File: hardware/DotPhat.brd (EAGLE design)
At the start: 30 x 65 mm, 17 parts, among them J2 RASPBERRYPI-40-PIN-GPIO_PTH, U1 ATMEGA328P-MU-QFN32

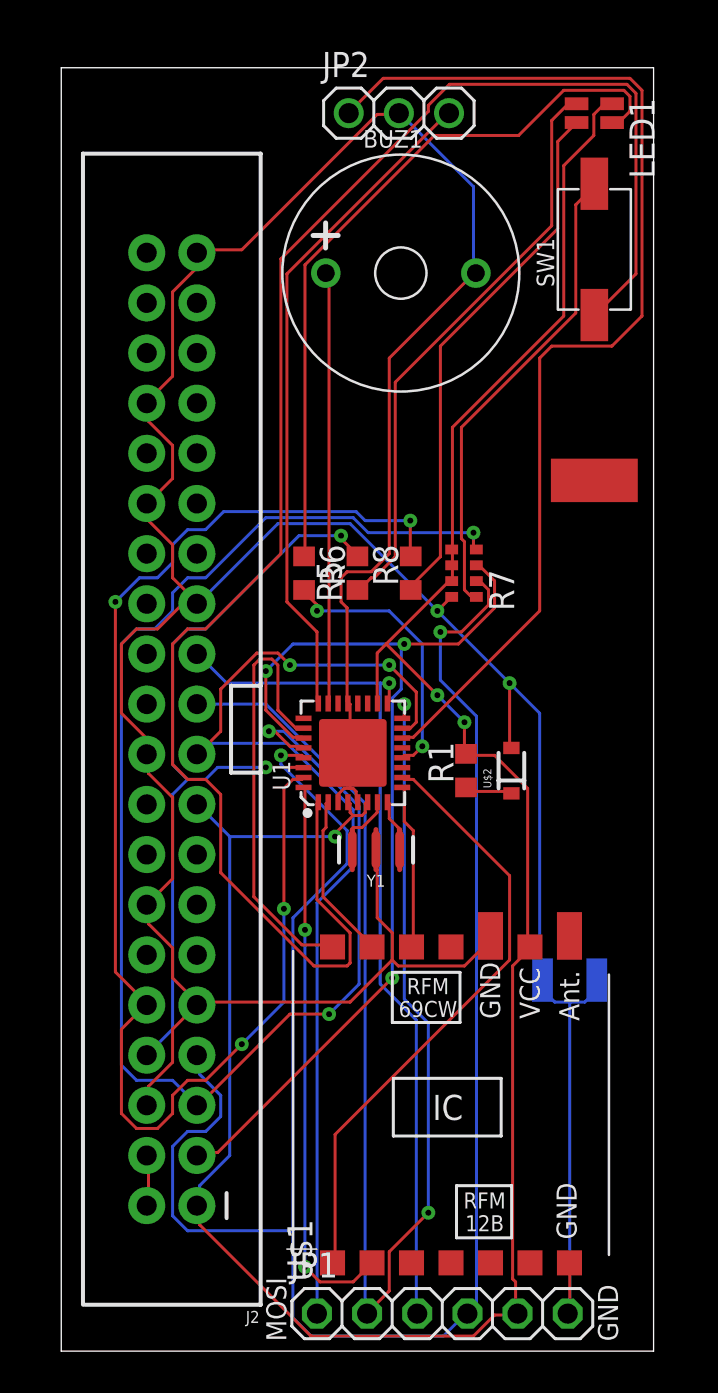
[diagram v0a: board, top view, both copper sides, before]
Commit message: Add 2 out JST connectors, solid GND vias
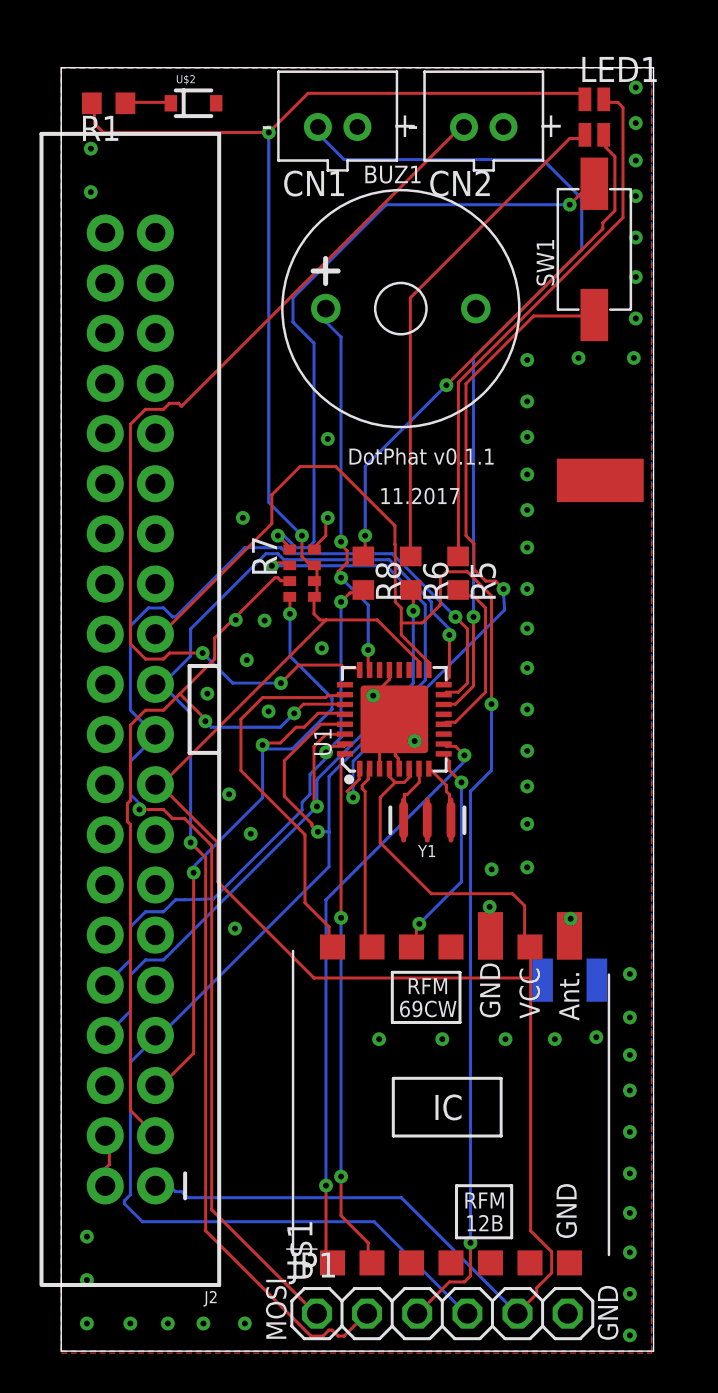
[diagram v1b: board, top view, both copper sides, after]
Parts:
- removed JP2: (no value), adafruit:1X03
- added CN1, CN2: (no value), adafruit:JST-PH-2-THM
- moved R1 38.3 mm to (2.40, 63.2), turned to 180 degrees
- moved U$2 37.4 mm to (6.70, 63.2), turned to 0 degrees
- moved R7 8.20 mm to (12.2, 39.4), turned to 270 degrees
- moved R5 7.80 mm to (20.1, 39.4)
- moved Y1 3.00 mm to (18.5, 26.9)
- moved U1 2.70 mm to (16.9, 32.0)
- moved R6 2.70 mm to (17.7, 39.4), turned to 270 degrees
- moved LOGO1 2.52 mm to (12.2, 44.1), turned to 0 degrees
- moved R8 2.40 mm to (15.3, 39.4), turned to 270 degrees
- moved J2 2.33 mm to (3.50, 32.5)
- moved BUZ1 1.80 mm to (17.2, 52.8)
- moved LED1 0.20 mm to (27.0, 62.5), turned to 0 degrees
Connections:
- net GND: now also CN1.1, CN2.1; no longer JP2.2
- net OUTA: now also CN1.2; no longer JP2.1
- net OUTB: now also CN2.2; no longer JP2.3
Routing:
- net GND: track 193.6 -> 11.0 mm, vias 2 -> 58
- net PUSH: track 87.0 -> 35.0 mm, vias 0 -> 2
- net TXD: track 70.3 -> 28.6 mm, vias 4 -> 2
- net SCL: track 76.3 -> 35.5 mm
- net +3V3: track 124.5 -> 153.1 mm, vias 3 -> 2
- net SCK: track 44.1 -> 71.1 mm, vias 1 -> 2
- net RST: track 98.7 -> 74.9 mm
- net OUTB: track 34.0 -> 47.6 mm, vias 0 -> 2
- net MOSI: track 53.5 -> 65.9 mm
- net OUTA: track 55.8 -> 43.9 mm, vias 0 -> 1
- net N$5: track 24.1 -> 33.7 mm, vias 0 -> 2
- net N$15: track 36.9 -> 27.4 mm
- net SDA: track 50.7 -> 43.0 mm
- net MISO: track 69.9 -> 63.3 mm
- net RXD: track 40.3 -> 34.6 mm
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- added copper zone on layer 1, net GND
- added copper zone on layer 16, net GND
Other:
- board text added: "11.2017"
- board text added: "DotPhat v0.1.1"

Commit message: Replace JST2 with JST4, add leds for channels
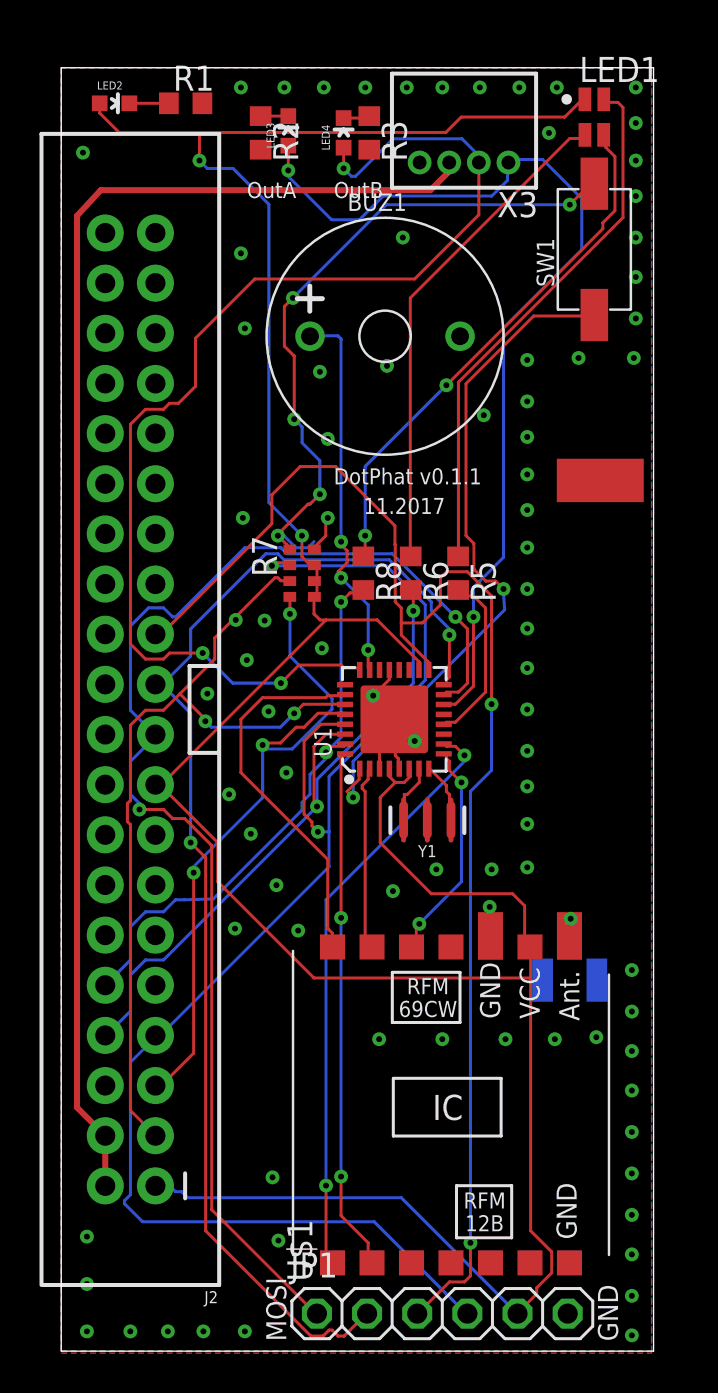
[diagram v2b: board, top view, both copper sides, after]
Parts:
- removed CN1, CN2: (no value), adafruit:JST-PH-2-THM
- removed U$2: DIODE-ZENER-BZT52, SparkFun:SOD-323
- added LED2, LED3, LED4: (no value), SparkFun:LED-0603
- added R2, R3: 250Ω, resistor:R0603
- added X3: S4B-ZR, con-jst:S4B-ZR
- R1: value (none) -> 250Ω
- moved R1 3.90 mm to (6.30, 63.2), turned to 0 degrees
- moved BUZ1 1.61 mm to (16.4, 51.4)
- moved LOGO1 1.39 mm to (10.9, 43.6)
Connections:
- removed net 5V: J2.2, J2.4
- new net +5V: J2.2, J2.4, X3.3
- new net N$7: LED3.C, R2.1
- new net N$9: LED4.C, R3.1
- net +3V3: now also LED2.A; no longer R1.2
- net GND: now also R1.2, R2.2, R3.2, X3.4; no longer CN1.1, CN2.1, U$2.2
- net N$2: now also LED2.C; no longer U$2.1
- net OUTA: now also LED3.A, X3.1; no longer CN1.2
- net OUTB: now also LED4.A, X3.2; no longer CN2.2
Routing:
- net +5V: track 0.00 -> 70.0 mm
- net OUTB: track 47.6 -> 60.0 mm, vias 2 -> 3
- net OUTA: track 43.9 -> 48.8 mm, vias 1 -> 2
- net 5V: track 2.73 -> 0.00 mm
- net +3V3: track 153.1 -> 154.9 mm
- net N$7: track 0.00 -> 1.40 mm
- net N$9: track 0.00 -> 1.34 mm
- net N$5: track 33.7 -> 34.8 mm, vias 2 -> 5
- net RST: track 74.9 -> 74.1 mm
- net GND: vias 58 -> 84
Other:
- board text added: "OutA"
- board text added: "OutB"

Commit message: amend
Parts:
- moved X1 1.40 mm to (25.8, 20.2)
- flipped LOGO1 to the top
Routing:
- net N$3: track 3.49 -> 2.09 mm
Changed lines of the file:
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@@
 <attribute name="MPN" value="ATMEGA328P-MU" x="16.87" y="32" size="1.778" layer="27" rot="R90" display="off"/>
 </element>
-<element name="X1" library="adafruit" package="U.FL" value="" x="25.75" y="18.79" rot="MR90"/>
+<element name="X1" library="adafruit" package="U.FL" value="" x="25.75" y="20.19" rot="MR90"/>
 <element name="Y1" library="SparkFun-Clocks" package="RESONATOR-SMD-3.2X1.3" value="" x="18.54" y="26.9" rot="R180"/>
 <element name="R5" library="resistor" package="R0603" value="67Ω" x="20.1" y="39.4" rot="R270"/>
@@
 <attribute name="MPN" value="KS-12065D03YA" x="16.4" y="51.4" size="1.778" layer="27" display="off"/>
 </element>
-<element name="LOGO1" library="Spark" package="OSHW-LOGO-S" value="OSHW-LOGOS" x="10.9" y="43.6" rot="MR0"/>
+<element name="LOGO1" library="Spark" package="OSHW-LOGO-S" value="OSHW-LOGOS" x="10.9" y="43.6"/>
 <element name="R1" library="resistor" package="R0603" value="250Ω" x="6.3" y="63.2"/>
 <element name="R7" library="SparkFun" package="0603-ARV" value="4.7kΩ" x="12.2" y="39.4" rot="R270"/>
@@
 <contactref element="U$1" pad="ANT"/>
 <contactref element="X1" pad="3"/>
-<wire x1="25.75" y1="20.315" x2="25.75" y2="21.95" width="0.1524" layer="16"/>
+<wire x1="25.75" y1="21.715" x2="25.75" y2="21.95" width="0.8128" layer="16"/>
 <wire x1="25.75" y1="21.95" x2="25.8" y2="21.9" width="0.1524" layer="16"/>
 <via x="25.8" y="21.9" extent="1-16" drill="0.3"/>
-<wire x1="25.8" y1="21.9" x2="25.8" y2="20.9696" width="0.1524" layer="1"/>
-<wire x1="25.8" y1="20.2" x2="25.8" y2="20.9696" width="0.1524" layer="1"/>
-<wire x1="25.8" y1="20.9696" x2="25.74" y2="21.0296" width="0.1524" layer="1"/>
+<wire x1="25.8" y1="21.9" x2="25.8" y2="21.9696" width="0.8128" layer="1"/>
+<wire x1="25.8" y1="21.2" x2="25.8" y2="21.9696" width="0.1524" layer="1"/>
+<wire x1="25.8" y1="21.9696" x2="25.74" y2="21.0296" width="0.1524" layer="1"/>
 </signal>
 <signal name="OUTA">

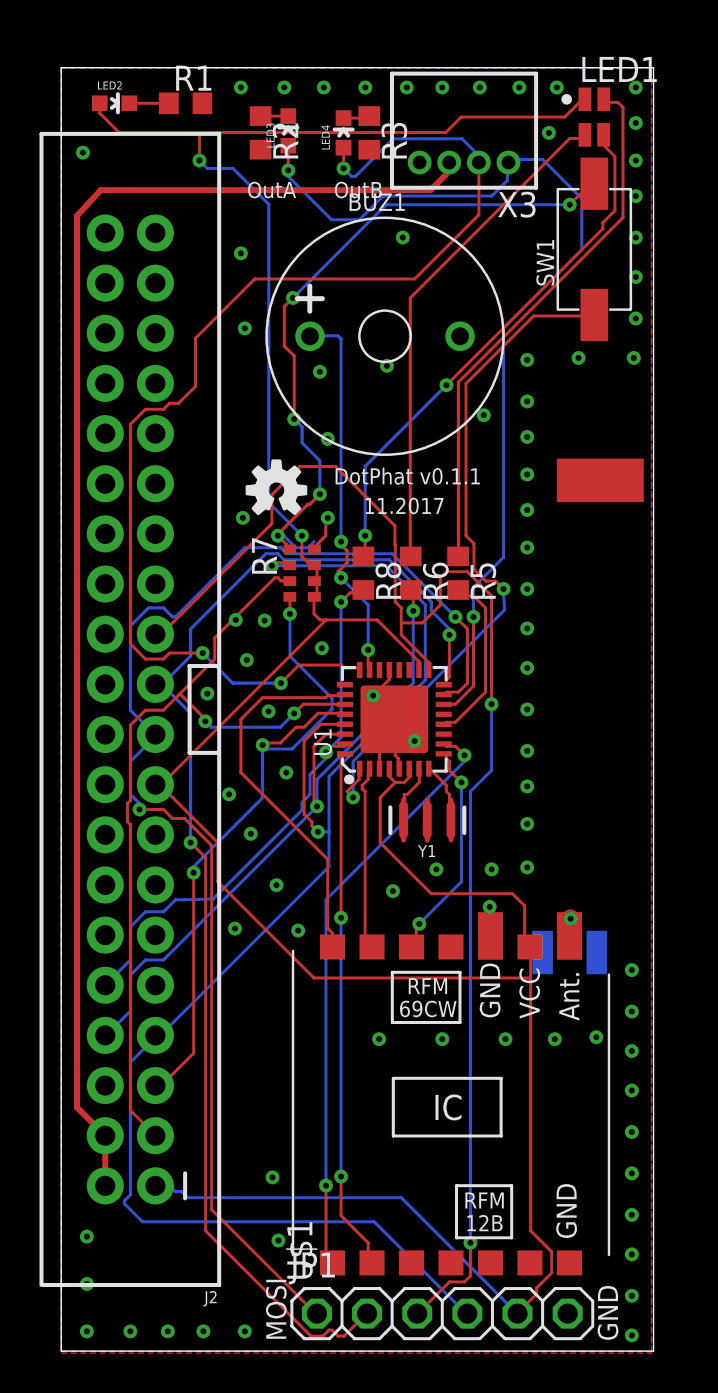
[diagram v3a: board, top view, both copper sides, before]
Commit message: Swap 5V and GND for the JST to match cable color
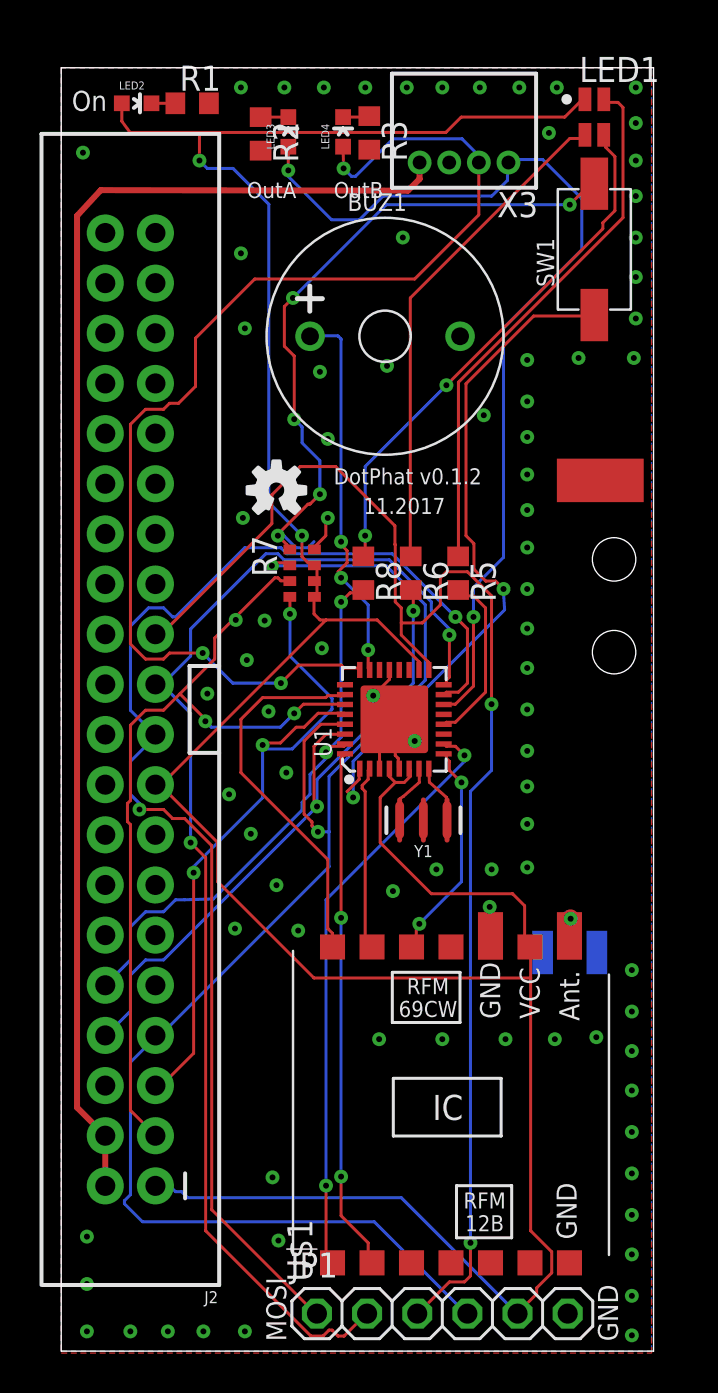
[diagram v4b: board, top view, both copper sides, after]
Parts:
- moved LED2 1.12 mm to (3.82, 63.2)
- moved R1 0.33 mm to (6.63, 63.2)
- moved Y1 0.20 mm to (18.3, 26.9)
- moved LED4 0.06 mm to (14.3, 61.8)
- moved R2 0.05 mm to (10.1, 61.6)
- moved LED3 0.05 mm to (11.5, 61.7)
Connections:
- net +5V: now also X3.4; no longer X3.3
- net GND: now also X3.3; no longer X3.4
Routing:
- net N$8: track 3.05 -> 4.40 mm
- net +5V: track 70.0 -> 68.7 mm
- net +3V3: track 154.9 -> 154.1 mm
- net N$2: track 2.00 -> 1.21 mm
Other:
- board text added: "DotPhat v0.1.2"
- board text added: "Mihai Galos"
- board text added: "On"
- board text removed: "DotPhat v0.1.1"
